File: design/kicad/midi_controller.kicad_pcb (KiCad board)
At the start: 4 copper layers, 166 x 166 mm, 123 parts, among them J1 Conn_01x05, J10 Conn_01x24_Socket, J2 Conn_01x02_Socket, J3 Conn_01x02_Socket, J4 Conn_01x02_Socket, J5 Conn_01x02_Socket, J6 Conn_01x02_Socket, J7 Conn_01x02_Socket, J9 Conn_01x24_Socket, U1 CD74HC4067M

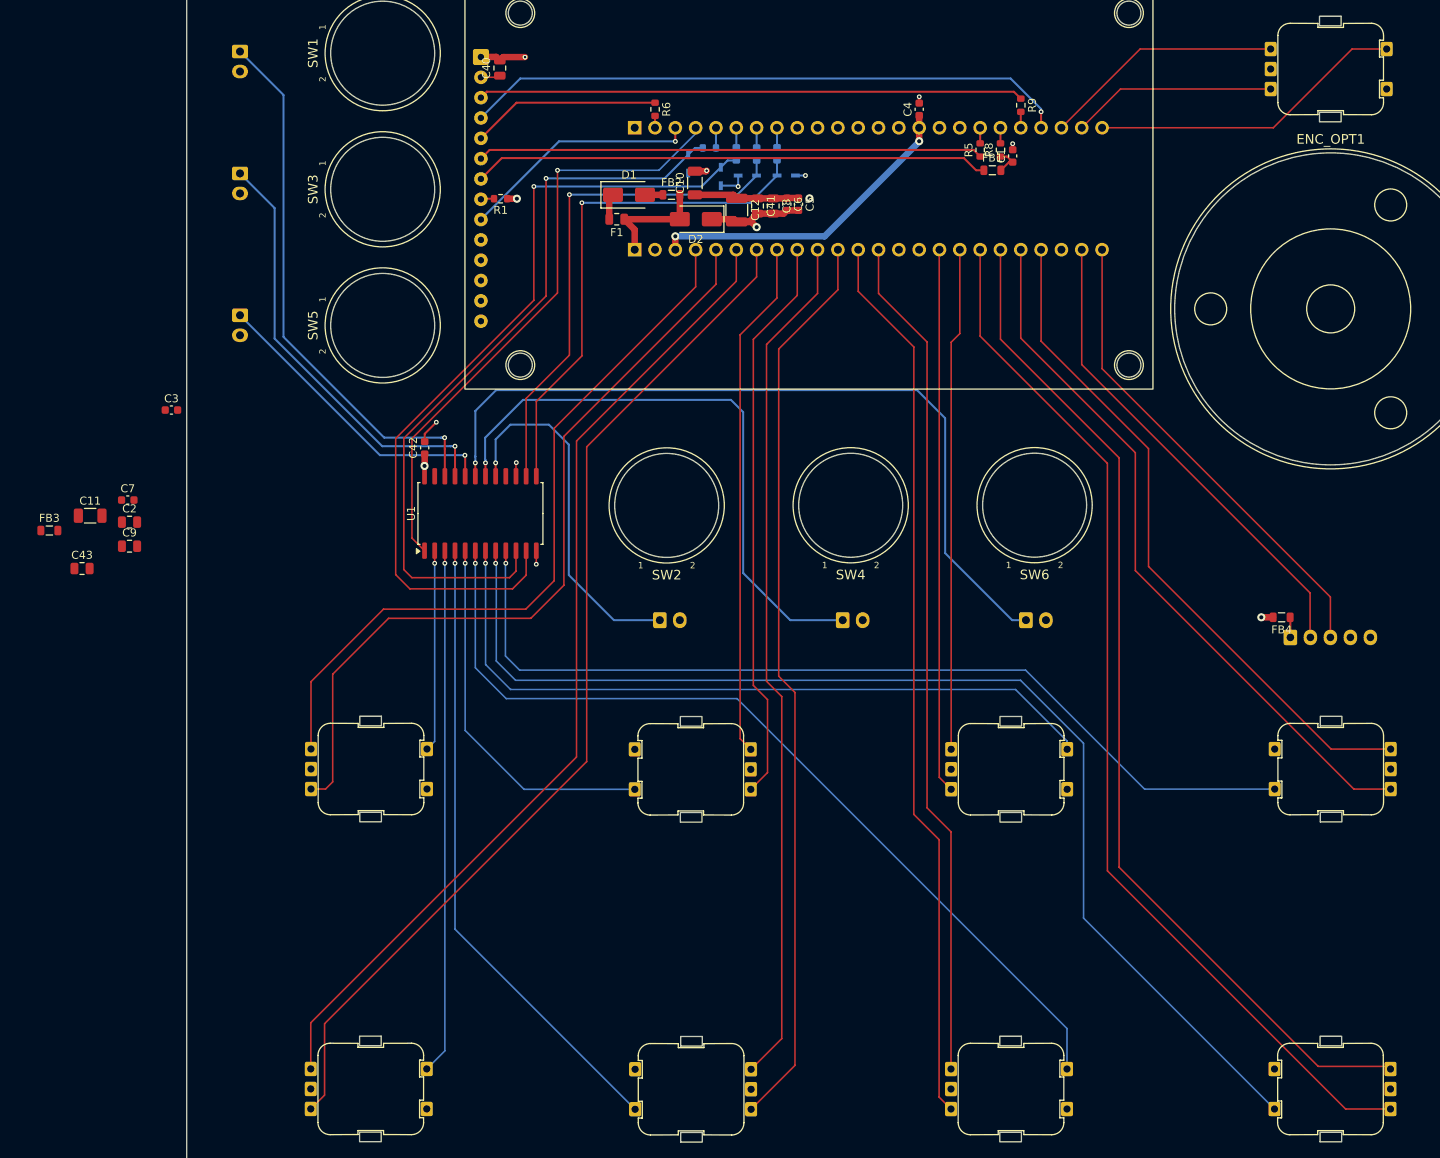
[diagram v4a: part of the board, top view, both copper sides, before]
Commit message: Update kicad binary files
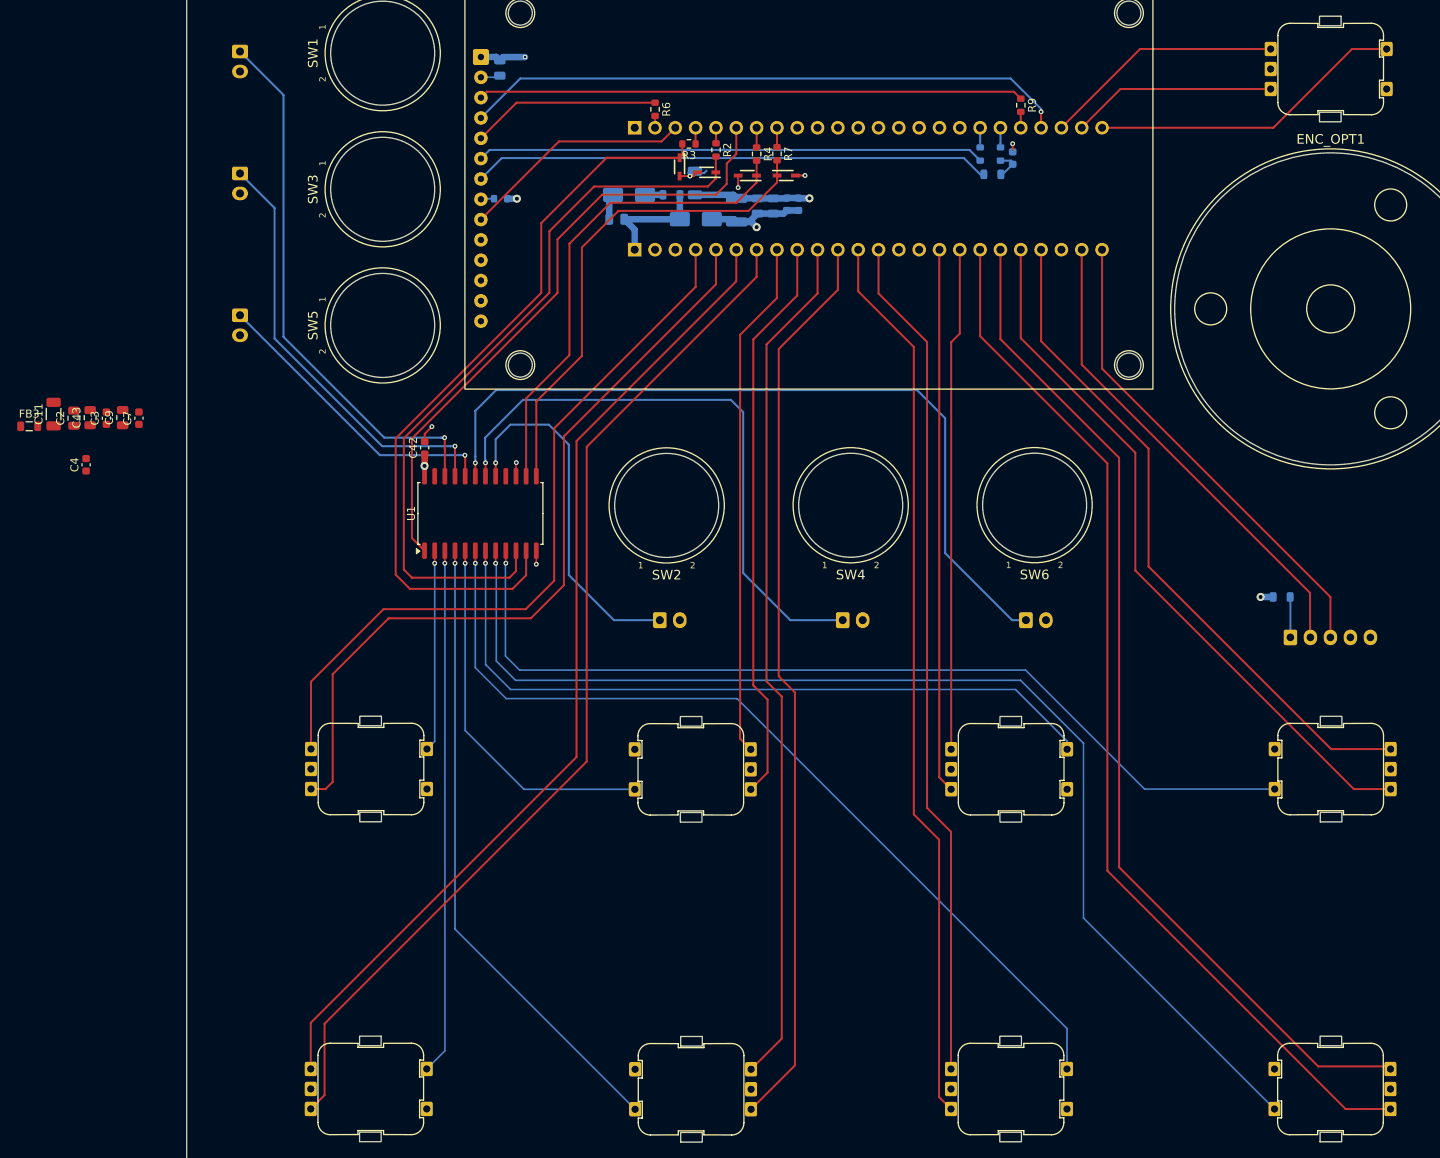
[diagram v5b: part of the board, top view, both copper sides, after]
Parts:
- C1, C10, C12, C40, C5, C6, C8, D1, D2, F1, FB1, FB2, FB4, R1, R5, R8: moved to B.Cu
- C41: value 10uF_0805_16V_lowESR -> 10u; moved to B.Cu
- D36, D37, D38, D39, R2, R3, R4, R7: moved to F.Cu
- moved C4 113.2 mm to (64.4, 142.0)
- moved C43 18.9 mm to (64.9, 136.1), turned to 90 degrees
- moved C9 16.1 mm to (69.0, 136.1), turned to 90 degrees
- moved C2 14.7 mm to (62.9, 136.1), turned to 90 degrees
- moved C11 13.5 mm to (60.4, 135.6), turned to 90 degrees
- moved FB3 13.3 mm to (57.3, 137.2)
- moved C7 10.3 mm to (71.0, 136.1), turned to 90 degrees
- moved C3 8.19 mm to (67.0, 136.1), turned to 90 degrees
- moved R3 6.05 mm to (139.8, 101.9), turned to 180 degrees
- moved D37 5.29 mm to (138.6, 104.7)
- moved FB4 2.54 mm to (213.9, 158.5)
- moved D36 2.53 mm to (142.0, 105.4), turned to 180 degrees
- moved R2 0.86 mm to (143.2, 102.6), turned to -90 degrees
- moved FB1 0.51 mm to (177.7, 105.7)
- moved R5 0.51 mm to (176.2, 103.1)
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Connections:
- net /Display MSP2807/LED renamed /LED
- C1 pad 1: /SCK -> Net-(C1-Pad1)
- DISP1 pad 7: /Display MSP2807/SCK -> /SCK
- FB1 pad 1: /Display MSP2807/SCK -> /SCK
- FB1 pad 2: /SCK -> Net-(C1-Pad1)
- J9 pad 2: /Teensy_4.1/T0 -> /DC
- J9 pad 4: /COM -> /S1
- J9 pad 5: /Teensy_4.1/T3 -> /S0
- J9 pad 6: /Teensy_4.1/T4 -> /COM
- J9 pad 7: /Teensy_4.1/T5 -> /S2
- J9 pad 8: /Teensy_4.1/T6 -> /S3
- R2 pad 1: /Teensy_4.1/T3 -> /S0
- R3 pad 1: /Teensy_4.1/T4 -> /S1
- R4 pad 1: /Teensy_4.1/T5 -> /S2
- R6 pad 2: /Teensy_4.1/T0 -> /DC
- R7 pad 1: /Teensy_4.1/T6 -> /S3
- R8 pad 1: /SCK -> Net-(C1-Pad1)
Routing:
- net /Display MSP2807/SCK: track 64.6 -> 0.00 mm
- net /SCK: track 3.78 -> 64.8 mm
- net +3V3: track 106.3 -> 66.0 mm, vias 4 -> 2
- net /S1: track 103.1 -> 97.6 mm, vias 1 -> 0
- net Net-(C1-Pad1): track 0.00 -> 3.87 mm
- net /COM: track 75.6 -> 78.7 mm, vias 1 -> 0
- net GND: track 33.5 -> 30.6 mm, vias 9 -> 8
- net Net-(J1-Pin_1): track 2.53 -> 5.07 mm
- net /Teensy_4.1/T3: track 2.53 -> 0.00 mm
- net /Teensy_4.1/T5: track 2.46 -> 0.00 mm
- net /Teensy_4.1/T4: track 2.44 -> 0.00 mm
- net /Teensy_4.1/T6: track 2.43 -> 0.00 mm
- net /DC: track 23.6 -> 25.1 mm
- net /Teensy_4.1/T0: track 1.48 -> 0.00 mm
- net /MISO: track 30.1 -> 29.1 mm, vias 1 -> 0
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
